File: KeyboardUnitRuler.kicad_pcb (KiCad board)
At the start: 2 copper layers, 246.7 x 19.1 mm, 24 parts

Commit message: Updated location of legends for better readability
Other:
- board text removed: "0u"

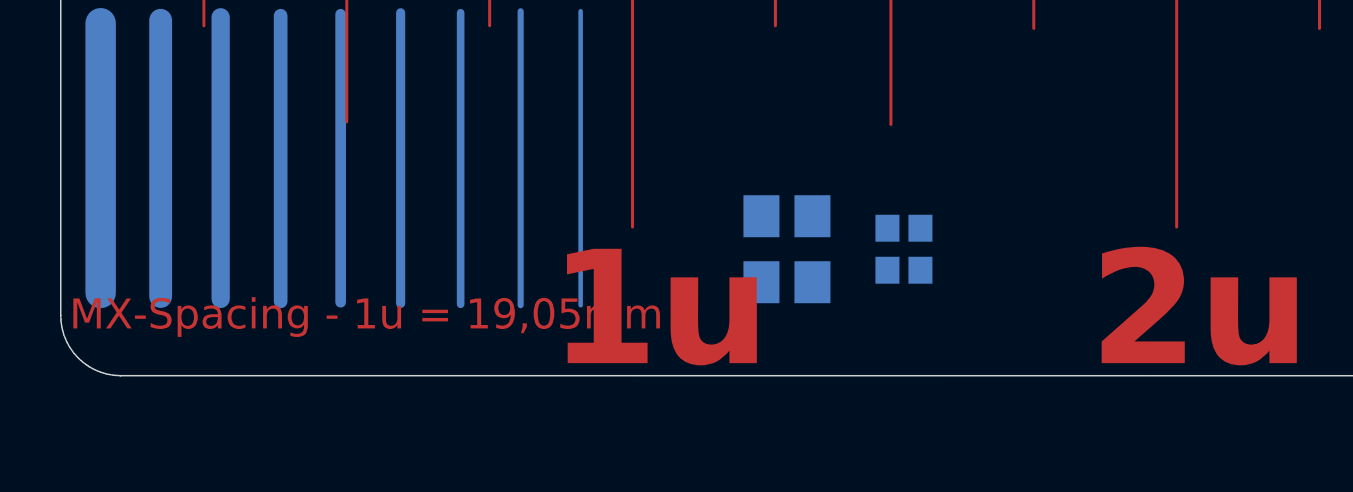
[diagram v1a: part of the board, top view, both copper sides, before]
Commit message: Better MX spacing graphic on the back and letters on the front.
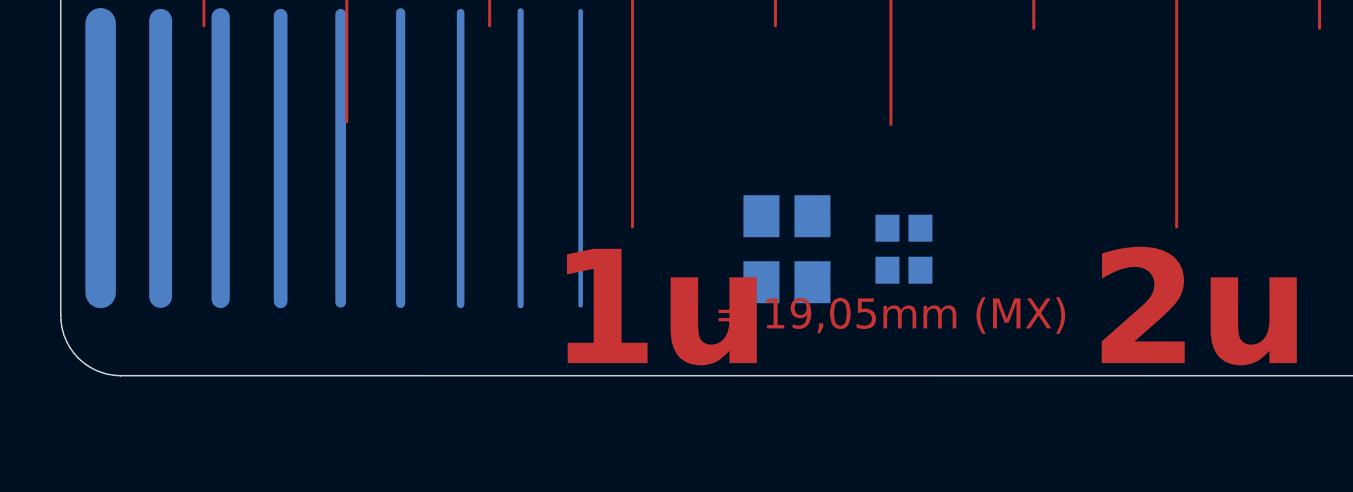
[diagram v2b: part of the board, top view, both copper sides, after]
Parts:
- removed the Ref** at (77.9, 71.3)
- added ? (x5): , Graphics, F.Cu at (96.5, 132.0)
- added ? (x5): , Graphics, F.Cu at (81.5, 94.0)
- added ?: , Graphics, B.Cu at (81.5, 94.0)
- added ?: , Graphics, B.Cu at (96.5, 132.0)
- added Ref**: Val**, TFL:mx spacing, B.Cu at (77.5, 71.3)
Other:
- board text added: "= 19,05mm (MX)"
- board text removed: "MX-Spacing - 1u = 19,05mm"
